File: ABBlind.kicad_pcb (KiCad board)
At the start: 2 copper layers, 99.1 x 53.3 mm, 23 parts, among them J1 JACK_FEMALE_STEREO_6_PINS, J2 JACK_FEMALE_STEREO_6_PINS, J3 JACK_FEMALE_STEREO_6_PINS, SW1 SW_PUSH, SW2 SW_PUSH, U1 TS5A22364, U2 TS5A22364, U3 TLV70033DDCT

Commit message: Routing almost finished
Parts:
- moved C5 3.22 mm to (157.6, 93.2)
- moved C4 3.14 mm to (157.7, 85.6)
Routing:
- net /AUDIO_CNTRL: track 0.00 -> 91.5 mm, vias 0 -> 2
- net GND: track 68.9 -> 137.2 mm, vias 0 -> 1
- net /RIGHT_OUT: track 52.6 -> 61.8 mm
- net +3V3: track 2.88 -> 10.7 mm
- net /GND_A: track 54.4 -> 55.9 mm
- net /LEFT_B: track 58.2 -> 56.9 mm
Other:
- board text added: "Put GND surface"

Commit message: Finish PCB routing
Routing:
- net /LEFT_B: track 56.9 -> 77.7 mm
- net /LEFT_OUT: track 16.7 -> 28.8 mm
- net /AUDIO_CNTRL: track 91.5 -> 100.3 mm
- net /GND_B: track 78.4 -> 83.9 mm
- net GND: track 137.2 -> 138.5 mm
- net /RIGHT_B: track 57.3 -> 58.3 mm
- net /FOOTSWITCH: track 63.3 -> 64.2 mm
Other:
- board text removed: "Put GND surface"

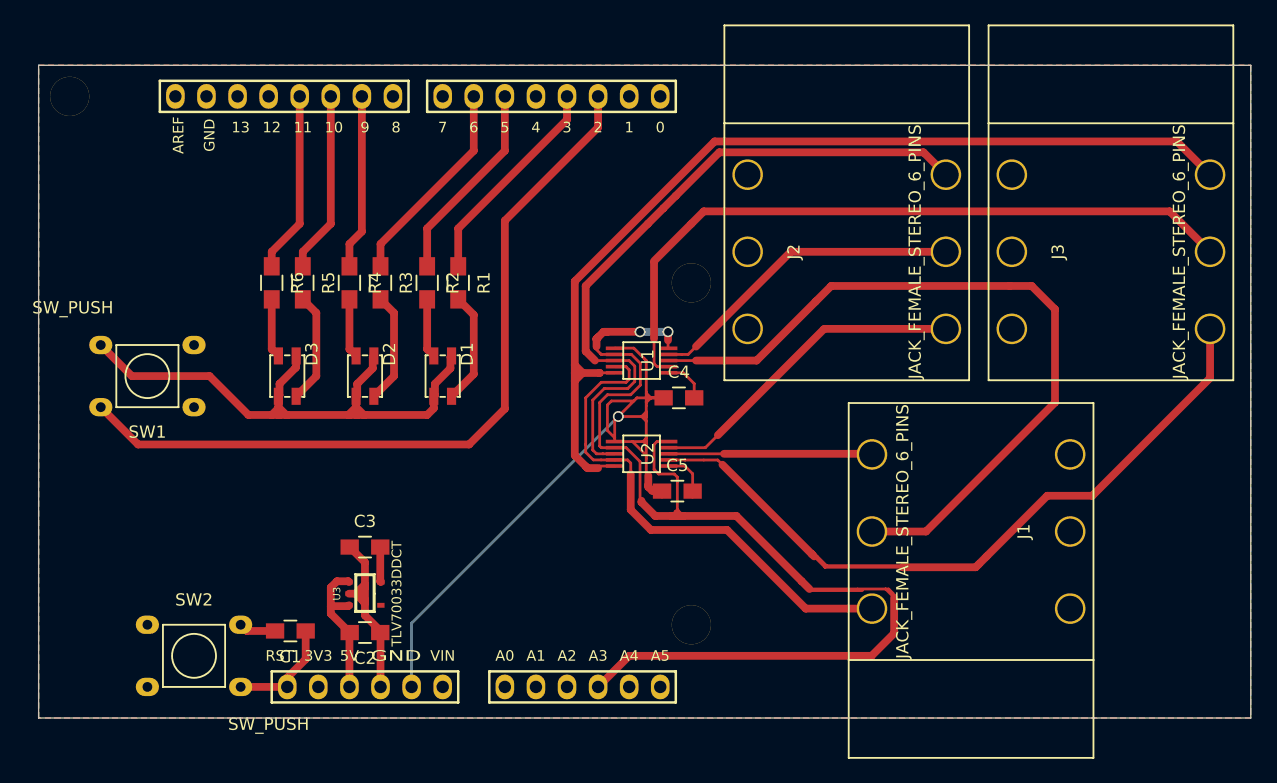
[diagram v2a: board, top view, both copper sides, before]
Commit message: Round edges
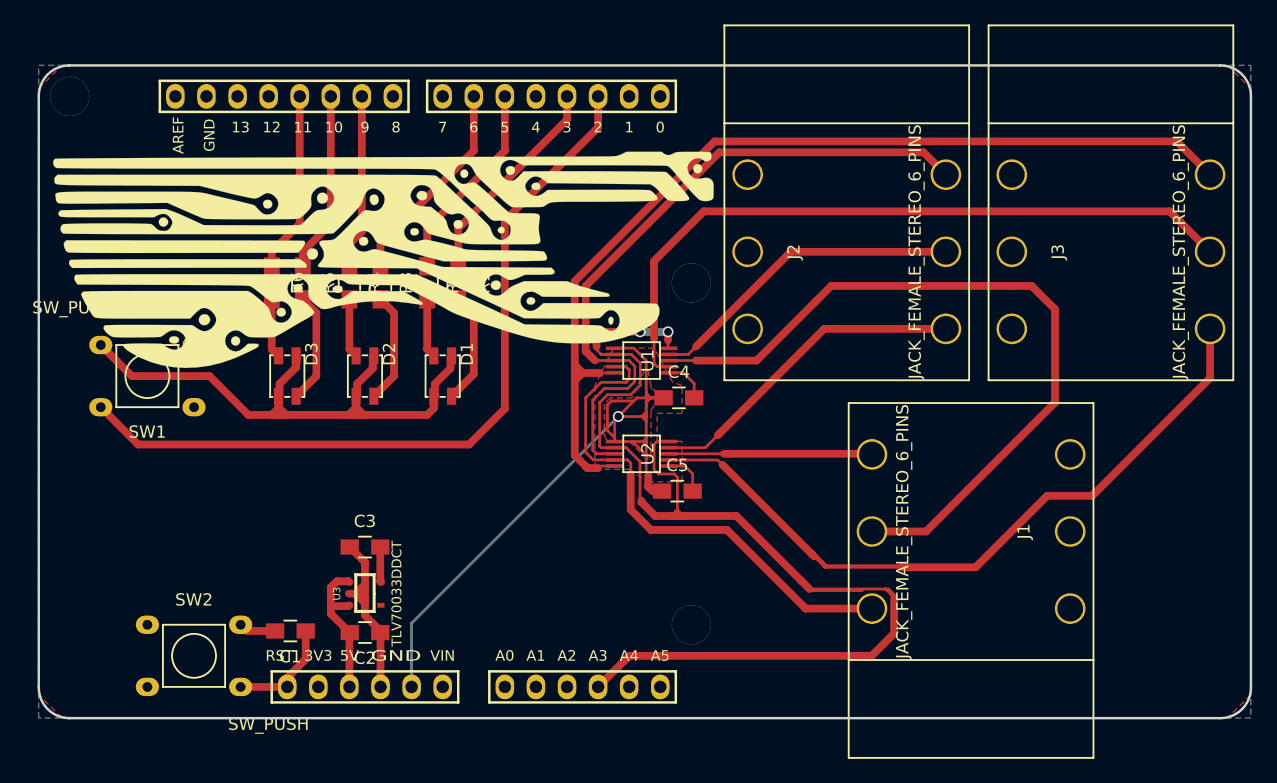
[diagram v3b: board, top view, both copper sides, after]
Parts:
- added G***: LOGO, def-footprints:logo_uc3music, B.Cu at (134.6, 91.4)
- added G***: LOGO, def-footprints:logo_guitar_uc3music, F.Cu at (133.3, 74.9)
- added G***: LOGO, def-footprints:logo_text_uc3music, B.Cu at (134.6, 68.6)
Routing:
- added copper zone on F.Cu, net GND
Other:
- outline, holes or cut-outs redrawn

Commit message: Prototype 1 - v0.1
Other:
- board text added: "A"
- board text added: "ABBlind Blind test pedal"
- board text added: "B"
- board text added: "David Estevez Fernandez"
- board text added: "OUT"
- board text added: "Prototype 1 - v0.1"
- board text added: "R6"

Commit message: Pre-fabrication v1.0
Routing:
- net /AUDIO_CNTRL: track 100.3 -> 103.0 mm
